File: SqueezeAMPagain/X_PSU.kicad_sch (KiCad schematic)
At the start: 1 part, among them J11 Conn_02x06_Odd_Even

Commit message: Update SqueezeAMPagain.kicad_pcb, SqueezeAMPagain.kicad_prl, SqueezeAMPagain.kicad_pro, and 7 more files
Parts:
- removed J11: Conn_02x06_Odd_Even, Connector_IDC:IDC-Header_2x06_P2.54mm_Vertical, symbol Connector_Generic:Conn_02x06_Odd_Even
- added J10: Conn_02x07_Odd_Even, Connector_IDC:IDC-Header_2x07_P2.54mm_Vertical, symbol Connector_Generic:Conn_02x07_Odd_Even
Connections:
- net +3.3V: now also J10.10 (Pin_10)
- net GND: now also J10.13 (Pin_13), J10.14 (Pin_14)
- net LV_ON: now also J10.8 (Pin_8)
- net PGND: now also J10.5 (Pin_5), J10.6 (Pin_6)
- net PON: now also J10.9 (Pin_9)
- net PVDD: now also J10.3 (Pin_3), J10.4 (Pin_4)
- net V_{IN}: now also J10.1 (Pin_1), J10.2 (Pin_2)
- net ~{WAKE}: now also J10.7 (Pin_7)
- new net SCL: J10.11 (Pin_11)
- new net SDA: J10.12 (Pin_12)
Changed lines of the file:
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@@
 	(wire
 		(pts
-			(xy 109.22 82.55) (xy 107.95 82.55)
+			(xy 109.22 85.09) (xy 107.95 85.09)
+		)
+		(stroke
+			(width 0)
+			(type default)
+		)
+	)
+	(wire
+		(pts
+			(xy 127 82.55) (xy 121.92 82.55)
 		)
 		(stroke
@@
 	(wire
 		(pts
-			(xy 121.92 82.55) (xy 124.46 82.55)
+			(xy 121.92 85.09) (xy 124.46 85.09)
 		)
 		(stroke
@@
 	(wire
 		(pts
-			(xy 124.46 82.55) (xy 124.46 85.09)
+			(xy 124.46 85.09) (xy 124.46 88.9)
 		)
 		(stroke
@@
 	(wire
 		(pts
+			(xy 105.41 82.55) (xy 109.22 82.55)
+		)
+		(stroke
+			(width 0)
+			(type default)
+		)
+	)
+	(wire
+		(pts
 			(xy 101.6 69.85) (xy 101.6 62.23)
 		)
@@
 	(wire
 		(pts
-			(xy 107.95 82.55) (xy 107.95 85.09)
+			(xy 107.95 85.09) (xy 107.95 87.63)
 		)
 		(stroke
@@
 		)
 	)
+	(hierarchical_label "SDA"
+		(shape bidirectional)
+		(at 127 82.55 0)
+		(fields_autoplaced yes)
+		(effects
+			(font
+				(size 1.27 1.27)
+			)
+			(justify left)
+		)
+	)
 	(hierarchical_label "LV_ON"
 		(shape input)
@@
 		)
 	)
+	(hierarchical_label "SCL"
+		(shape input)
+		(at 105.41 82.55 180)
+		(fields_autoplaced yes)
+		(effects
+			(font
+				(size 1.27 1.27)
+			)
+			(justify right)
+		)
+	)
 	(hierarchical_label "PON"
 		(shape input)
@@
 	)
 	(symbol
-		(lib_id "Connector_Generic:Conn_02x06_Odd_Even")
-		(at 114.3 74.93 0)
+		(lib_id "Connector_Generic:Conn_02x07_Odd_Even")
+		(at 114.3 77.47 0)
 		(unit 1)
 		(exclude_from_sim no)
@@
 		(dnp no)
 		(fields_autoplaced yes)
-		(property "Reference" "J11"
+		(property "Reference" "J10"
 			(at 115.57 63.5 0)
 			(effects
@@
 			)
 		)
-		(property "Value" "Conn_02x06_Odd_Even"
+		(property "Value" "Conn_02x07_Odd_Even"
 			(at 115.57 66.04 0)
 			(effects
@@
 			)
 		)
-		(property "Footprint" "Connector_IDC:IDC-Header_2x06_P2.54mm_Vertical"
-			(at 114.3 74.93 0)
+		(property "Footprint" "Connector_IDC:IDC-Header_2x07_P2.54mm_Vertical"
+			(at 114.3 77.47 0)
 			(effects
 				(font
@@
 		)
 		(property "Datasheet" "~"
-			(at 114.3 74.93 0)
-			(effects
-				(font
-					(size 1.27 1.27)
-				)
-				(hide yes)
-			)
-		)
-		(property "Description" "Generic connector, double row, 02x06, odd/even pin numbering scheme (row 1 odd numbers, row 2 even numbers), script generated (kicad-library-utils/schlib/autogen/connector/)"
-			(at 114.3 74.93 0)
-			(effects
-				(font
-					(size 1.27 1.27)
-				)
-				(hide yes)
-			)
+			(at 114.3 77.47 0)
+			(effects
+				(font
+					(size 1.27 1.27)
+				)
+				(hide yes)
+			)
+		)
+		(property "Description" "Generic connector, double row, 02x07, odd/even pin numbering scheme (row 1 odd numbers, row 2 even numbers), script generated (kicad-library-utils/schlib/autogen/connector/)"
+			(at 114.3 77.47 0)
+			(effects
+				(font
+					(size 1.27 1.27)
+				)
+				(hide yes)
+			)
+		)
+		(property "reichelt#" "BKL 10120556"
+			(at 114.3 77.47 0)
+			(effects
+				(font
+					(size 1.27 1.27)
+				)
+				(hide yes)
+			)
+		)
+		(pin "13"
+		)
+		(pin "5"
 		)
 		(pin "7"
 		)
-		(pin "5"
+		(pin "6"
+		)
+		(pin "10"
+		)
+		(pin "1"
+		)
+		(pin "3"
+		)
+		(pin "11"
+		)
+		(pin "8"
+		)
+		(pin "12"
 		)
 		(pin "4"
 		)
-		(pin "11"
-		)
-		(pin "8"
-		)
-		(pin "6"
-		)
 		(pin "9"
 		)
 		(pin "2"
 		)
-		(pin "10"
-		)
-		(pin "3"
-		)
-		(pin "12"
-		)
-		(pin "1"
+		(pin "14"
 		)
 		(instances
 			(project ""
 				(path "/3675160b-d9e5-490e-b506-2a7966e79ed0/ebd96d54-3bca-4cd9-8a7f-03e0b2610c15"
-					(reference "J11")
+					(reference "J10")
 					(unit 1)
 				)
@@
 	(symbol
 		(lib_id "power:GND")
-		(at 107.95 85.09 0)
+		(at 107.95 87.63 0)
 		(unit 1)
 		(exclude_from_sim no)
@@
 		(dnp no)
 		(property "Reference" "#PWR0116"
-			(at 107.95 91.44 0)
+			(at 107.95 93.98 0)
 			(effects
 				(font
@@
 		)
 		(property "Value" "GND"
-			(at 108.204 89.154 0)
+			(at 108.204 91.694 0)
 			(effects
 				(font
@@
 		)
 		(property "Footprint" ""
-			(at 107.95 85.09 0)
+			(at 107.95 87.63 0)
 			(effects
 				(font
@@
 		)
 		(property "Datasheet" ""
-			(at 107.95 85.09 0)
+			(at 107.95 87.63 0)
 			(effects
 				(font
@@
 		)
 		(property "Description" "Power symbol creates a global label with name \"GND\" , ground"
-			(at 107.95 85.09 0)
+			(at 107.95 87.63 0)
 			(effects
 				(font
@@
 	(symbol
 		(lib_id "power:GND")
-		(at 124.46 85.09 0)
+		(at 124.46 88.9 0)
 		(unit 1)
 		(exclude_from_sim no)
@@
 		(dnp no)
 		(property "Reference" "#PWR0117"
-			(at 124.46 91.44 0)
+			(at 124.46 95.25 0)
 			(effects
 				(font
@@
 		)
 		(property "Value" "GND"
-			(at 124.714 89.154 0)
+			(at 124.714 92.964 0)
 			(effects
 				(font
@@
 		)
 		(property "Footprint" ""
-			(at 124.46 85.09 0)
+			(at 124.46 88.9 0)
 			(effects
 				(font
@@
 		)
 		(property "Datasheet" ""
-			(at 124.46 85.09 0)
+			(at 124.46 88.9 0)
 			(effects
 				(font
@@
 		)
 		(property "Description" "Power symbol creates a global label with name \"GND\" , ground"
-			(at 124.46 85.09 0)
-			(effects
-				(font
+			(at 124.46 88.9 0)
+			(effects
+				(font

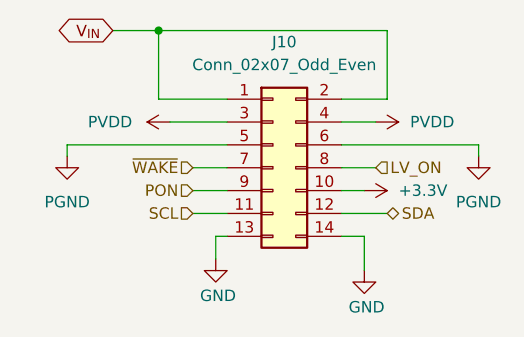
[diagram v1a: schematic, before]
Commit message: Update SqueezeAMPagain.kicad_pcb, SqueezeAMPagain.kicad_prl, SqueezeAMPagain.kicad_pro, and 5 more files
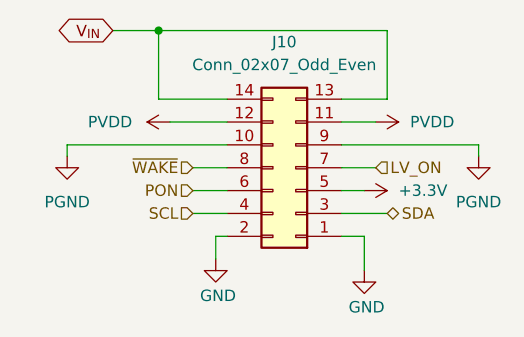
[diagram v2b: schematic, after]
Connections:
- net +3.3V: now also J10.5 (Pin_5); no longer J10.10 (Pin_10)
- net GND: now also J10.1 (Pin_1), J10.2 (Pin_2); no longer J10.13 (Pin_13), J10.14 (Pin_14)
- net LV_ON: now also J10.7 (Pin_7); no longer J10.8 (Pin_8)
- net PGND: now also J10.10 (Pin_10), J10.9 (Pin_9); no longer J10.5 (Pin_5), J10.6 (Pin_6)
- net PON: now also J10.6 (Pin_6); no longer J10.9 (Pin_9)
- net PVDD: now also J10.11 (Pin_11), J10.12 (Pin_12); no longer J10.3 (Pin_3), J10.4 (Pin_4)
- net SCL: now also J10.4 (Pin_4); no longer J10.11 (Pin_11)
- net SDA: now also J10.3 (Pin_3); no longer J10.12 (Pin_12)
- net V_{IN}: now also J10.13 (Pin_13), J10.14 (Pin_14); no longer J10.1 (Pin_1), J10.2 (Pin_2)
- net ~{WAKE}: now also J10.8 (Pin_8); no longer J10.7 (Pin_7)
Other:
- moved on the sheet: J10
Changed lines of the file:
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@@
 	(symbol
 		(lib_id "Connector_Generic:Conn_02x07_Odd_Even")
-		(at 114.3 77.47 0)
+		(at 116.84 77.47 180)
 		(unit 1)
 		(exclude_from_sim no)
@@
 		)
 		(property "Footprint" "Connector_IDC:IDC-Header_2x07_P2.54mm_Vertical"
-			(at 114.3 77.47 0)
+			(at 116.84 77.47 0)
 			(effects
 				(font
@@
 		)
 		(property "Datasheet" "~"
-			(at 114.3 77.47 0)
+			(at 116.84 77.47 0)
 			(effects
 				(font
@@
 		)
 		(property "Description" "Generic connector, double row, 02x07, odd/even pin numbering scheme (row 1 odd numbers, row 2 even numbers), script generated (kicad-library-utils/schlib/autogen/connector/)"
-			(at 114.3 77.47 0)
+			(at 116.84 77.47 0)
 			(effects
 				(font
@@
 		)
 		(property "reichelt#" "BKL 10120556"
-			(at 114.3 77.47 0)
+			(at 116.84 77.47 0)
 			(effects
 				(font

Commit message: Update SqueezeAMPagain.kicad_pcb, SqueezeAMPagain.kicad_prl, SqueezeAMPagain.kicad_pro, and 4 more files
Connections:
- net +3.3V: now also J10.10 (Pin_10); no longer J10.5 (Pin_5)
- net GND: now also J10.13 (Pin_13), J10.14 (Pin_14); no longer J10.1 (Pin_1), J10.2 (Pin_2)
- net LV_ON: now also J10.8 (Pin_8); no longer J10.7 (Pin_7)
- net PGND: now also J10.5 (Pin_5), J10.6 (Pin_6); no longer J10.10 (Pin_10), J10.9 (Pin_9)
- net PON: now also J10.9 (Pin_9); no longer J10.6 (Pin_6)
- net PVDD: now also J10.3 (Pin_3), J10.4 (Pin_4); no longer J10.11 (Pin_11), J10.12 (Pin_12)
- net SCL: now also J10.11 (Pin_11); no longer J10.4 (Pin_4)
- net SDA: now also J10.12 (Pin_12); no longer J10.3 (Pin_3)
- net V_{IN}: now also J10.1 (Pin_1); no longer J10.13 (Pin_13), J10.14 (Pin_14)
- net ~{WAKE}: now also J10.7 (Pin_7); no longer J10.8 (Pin_8)
- new net V_{USB}: J10.2 (Pin_2)
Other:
- moved on the sheet: J10

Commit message: Update SqueezeAMPagain.kicad_pcb, SqueezeAMPagain.kicad_prl, SqueezeAMPagain.kicad_pro, and 5 more files
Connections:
- net PVDD is gone; now on net V_{IN}: J10.3 (Pin_3), J10.4 (Pin_4)
- net V_{IN}: no longer J10.1 (Pin_1)
- new net V_{supply}: J10.1 (Pin_1)
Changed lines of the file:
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@@
+		)
+	)
+	(global_label "V_{supply}"
+		(shape input)
+		(at 109.22 90.17 180)
+		(fields_autoplaced yes)
+		(effects
+			(font
+				(size 1.27 1.27)
+			)
+			(justify right)
+		)
+		(property "Intersheetrefs" "${INTERSHEET_REFS}"
+			(at 100.209 90.17 0)
+			(effects
+				(font
+					(size 1.27 1.27)
+				)
+				(justify right)
+				(hide yes)
+			)
 		)
 	)
@@
 	)
 	(global_label "V_{IN}"
-		(shape bidirectional)
-		(at 109.22 90.17 180)
+		(shape output)
+		(at 148.59 92.71 0)
+		(fields_autoplaced yes)
+		(effects
+			(font
+				(size 1.27 1.27)
+			)
+			(justify left)
+		)
+		(property "Intersheetrefs" "${INTERSHEET_REFS}"
+			(at 154.2628 92.71 0)
+			(effects
+				(font
+					(size 1.27 1.27)
+				)
+				(justify left)
+				(hide yes)
+			)
+		)
+	)
+	(global_label "V_{IN}"
+		(shape output)
+		(at 125.73 92.71 180)
 		(fields_autoplaced yes)
 		(effects
@@
 		)
 		(property "Intersheetrefs" "${INTERSHEET_REFS}"
-			(at 102.4359 90.17 0)
+			(at 120.0572 92.71 0)
 			(effects
 				(font
@@
 	)
 	(symbol
-		(lib_id "power:+24V")
-		(at 148.59 92.71 270)
-		(unit 1)
-		(exclude_from_sim no)
-		(in_bom yes)
-		(on_board yes)
-		(dnp no)
-		(fields_autoplaced yes)
-		(property "Reference" "#PWR0119"
-			(at 144.78 92.71 0)
-			(effects
-				(font
-					(size 1.27 1.27)
-				)
-				(hide yes)
-			)
-		)
-		(property "Value" "PVDD"
-			(at 152.4 92.7099 90)
-			(effects
-				(font
-					(size 1.27 1.27)
-				)
-				(justify left)
-			)
-		)
-		(property "Footprint" ""
-			(at 148.59 92.71 0)
-			(effects
-				(font
-					(size 1.27 1.27)
-				)
-				(hide yes)
-			)
-		)
-		(property "Datasheet" ""
-			(at 148.59 92.71 0)
-			(effects
-				(font
-					(size 1.27 1.27)
-				)
-				(hide yes)
-			)
-		)
-		(property "Description" "Power symbol creates a global label with name \"+24V\""
-			(at 148.59 92.71 0)
-			(effects
-				(font
-					(size 1.27 1.27)
-				)
-				(hide yes)
-			)
-		)
-		(pin "1"
-		)
-		(instances
-			(project "SqueezeAMPagain"
-				(path "/3675160b-d9e5-490e-b506-2a7966e79ed0/ebd96d54-3bca-4cd9-8a7f-03e0b2610c15"
-					(reference "#PWR0119")
-					(unit 1)
-				)
-			)
-		)
-	)
-	(symbol
 		(lib_id "power:GND")
 		(at 147.32 109.22 0)
@@
 					(unit 1)
 				)
-			)
-		)
-	)
-	(symbol
-		(lib_id "power:+24V")
-		(at 125.73 92.71 90)
-		(unit 1)
-		(exclude_from_sim no)
-		(in_bom yes)
-		(on_board yes)
-		(dnp no)
-		(fields_autoplaced yes)
-		(property "Reference" "#PWR0115"
-			(at 129.54 92.71 0)
-			(effects
-				(font
-					(size 1.27 1.27)
-				)
-				(hide yes)
-			)
-		)
-		(property "Value" "PVDD"
-			(at 121.531 92.7099 90)
-			(effects
-				(font
-					(size 1.27 1.27)
-				)
-				(justify left)
-			)
-		)
-		(property "Footprint" ""
-			(at 125.73 92.71 0)
-			(effects
-				(font
-					(size 1.27 1.27)
-				)
-				(hide yes)
-			)
-		)
-		(property "Datasheet" ""
-			(at 125.73 92.71 0)
-			(effects
-				(font
-					(size 1.27 1.27)
-				)
-				(hide yes)
-			)
-		)
-		(property "Description" "Power symbol creates a global label with name \"+24V\""
-			(at 125.73 92.71 0)
-			(effects
-				(font
-					(size 1.27 1.27)
-				)
-				(hide yes)
-			)
-		)
-		(pin "1"
-		)
-		(instances
-			(project "SqueezeAMPagain"
-				(path "/3675160b-d9e5-490e-b506-2a7966e79ed0/ebd96d54-3bca-4cd9-8a7f-03e0b2610c15"
-					(reference "#PWR0115")
-					(unit 1)
-				)

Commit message: Update SqueezeAMPagain.kicad_pcb, SqueezeAMPagain.kicad_prl, SqueezeAMPagain.kicad_pro, and 11 more files
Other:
- note added: "Power expansion connector"
- title: (none) -> SqueezeAMP_{again}
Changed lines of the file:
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@@
 	(generator_version "8.0")
 	(paper "A4")
-	(wire
-		(pts
-			(xy 125.73 92.71) (xy 132.08 92.71)
+	(title_block
+		(title "SqueezeAMP_{again}")
+		(date "2024-08-23")
+		(rev "1.0")
+	)
+	(wire
+		(pts
+			(xy 119.38 92.71) (xy 132.08 92.71)
 		)
 		(stroke
@@
 	(wire
 		(pts
-			(xy 132.08 105.41) (xy 130.81 105.41)
+			(xy 132.08 105.41) (xy 129.54 105.41)
 		)
 		(stroke
@@
 	(wire
 		(pts
-			(xy 114.3 96.52) (xy 114.3 95.25)
+			(xy 101.6 96.52) (xy 101.6 95.25)
 		)
 		(stroke
@@
 	(wire
 		(pts
-			(xy 160.02 95.25) (xy 144.78 95.25)
-		)
-		(stroke
-			(width 0)
-			(type default)
-		)
-	)
-	(wire
-		(pts
-			(xy 114.3 95.25) (xy 132.08 95.25)
-		)
-		(stroke
-			(width 0)
-			(type default)
-		)
-	)
-	(wire
-		(pts
-			(xy 144.78 92.71) (xy 148.59 92.71)
-		)
-		(stroke
-			(width 0)
-			(type default)
-		)
-	)
-	(wire
-		(pts
-			(xy 160.02 96.52) (xy 160.02 95.25)
-		)
-		(stroke
-			(width 0)
-			(type default)
-		)
-	)
-	(wire
-		(pts
-			(xy 130.81 105.41) (xy 130.81 109.22)
-		)
-		(stroke
-			(width 0)
-			(type default)
+			(xy 179.07 95.25) (xy 144.78 95.25)
+		)
+		(stroke
+			(width 0)
+			(type default)
+		)
+	)
+	(wire
+		(pts
+			(xy 101.6 95.25) (xy 132.08 95.25)
+		)
+		(stroke
+			(width 0)
+			(type default)
+		)
+	)
+	(wire
+		(pts
+			(xy 144.78 92.71) (xy 157.48 92.71)
+		)
+		(stroke
+			(width 0)
+			(type default)
+		)
+	)
+	(wire
+		(pts
+			(xy 179.07 96.52) (xy 179.07 95.25)
+		)
+		(stroke
+			(width 0)
+			(type default)
+		)
+	)
+	(wire
+		(pts
+			(xy 129.54 105.41) (xy 129.54 109.22)
+		)
+		(stroke
+			(width 0)
+			(type default)
+		)
+	)
+	(text "Power expansion connector"
+		(exclude_from_sim no)
+		(at 138.43 73.406 0)
+		(effects
+			(font
+				(size 1.27 1.27)
+			)
 		)
 	)
@@
 	(global_label "V_{IN}"
 		(shape output)
-		(at 148.59 92.71 0)
+		(at 157.48 92.71 0)
 		(fields_autoplaced yes)
 		(effects
@@
 		)
 		(property "Intersheetrefs" "${INTERSHEET_REFS}"
-			(at 154.2628 92.71 0)
+			(at 163.1528 92.71 0)
 			(effects
 				(font
@@
 	(global_label "V_{IN}"
 		(shape output)
-		(at 125.73 92.71 180)
+		(at 119.38 92.71 180)
 		(fields_autoplaced yes)
 		(effects
@@
 		)
 		(property "Intersheetrefs" "${INTERSHEET_REFS}"
-			(at 120.0572 92.71 0)
+			(at 113.7072 92.71 0)
 			(effects
 				(font
@@
 	(symbol
 		(lib_id "power:GND1")
-		(at 114.3 96.52 0)
+		(at 101.6 96.52 0)
 		(unit 1)
 		(exclude_from_sim no)
@@
 		(fields_autoplaced yes)
 		(property "Reference" "#PWR0114"
-			(at 114.3 102.87 0)
+			(at 101.6 102.87 0)
 			(effects
 				(font
@@
 		)
 		(property "Value" "PGND"
-			(at 114.3 101.6 0)
+			(at 101.6 101.6 0)
 			(effects
 				(font
@@
 		)
 		(property "Footprint" ""
-			(at 114.3 96.52 0)
+			(at 101.6 96.52 0)
 			(effects
 				(font
@@
 		)
 		(property "Datasheet" ""
-			(at 114.3 96.52 0)
+			(at 101.6 96.52 0)
 			(effects
 				(font
@@
 		)
 		(property "Description" "Power symbol creates a global label with name \"GND1\" , ground"
-			(at 114.3 96.52 0)
+			(at 101.6 96.52 0)
 			(effects
 				(font
@@
 	(symbol
 		(lib_id "power:GND")
-		(at 130.81 109.22 0)
+		(at 129.54 109.22 0)
 		(unit 1)
 		(exclude_from_sim no)
@@
 		(dnp no)
 		(property "Reference" "#PWR0116"
-			(at 130.81 115.57 0)
+			(at 129.54 115.57 0)
 			(effects
 				(font
@@
 		)
 		(property "Value" "GND"
-			(at 131.064 113.284 0)
+			(at 129.794 113.284 0)
 			(effects
 				(font
@@
 		)
 		(property "Footprint" ""
-			(at 130.81 109.22 0)
+			(at 129.54 109.22 0)
 			(effects
 				(font
@@
 		)
 		(property "Datasheet" ""
-			(at 130.81 109.22 0)
+			(at 129.54 109.22 0)
 			(effects
 				(font
@@
 		)
 		(property "Description" "Power symbol creates a global label with name \"GND\" , ground"
-			(at 130.81 109.22 0)
+			(at 129.54 109.22 0)
 			(effects
 				(font
@@
 	(symbol
 		(lib_id "power:GND1")
-		(at 160.02 96.52 0)
+		(at 179.07 96.52 0)
 		(unit 1)
 		(exclude_from_sim no)
@@
 		(fields_autoplaced yes)
 		(property "Reference" "#PWR0120"
-			(at 160.02 102.87 0)
+			(at 179.07 102.87 0)
 			(effects
 				(font
@@
 		)
 		(property "Value" "PGND"
-			(at 160.02 101.6 0)
+			(at 179.07 101.6 0)
 			(effects
 				(font
@@
 		)
 		(property "Footprint" ""
-			(at 160.02 96.52 0)
+			(at 179.07 96.52 0)
 			(effects
 				(font
@@
 		)
 		(property "Datasheet" ""
-			(at 160.02 96.52 0)
+			(at 179.07 96.52 0)
 			(effects
 				(font
@@
 		)
 		(property "Description" "Power symbol creates a global label with name \"GND1\" , ground"
-			(at 160.02 96.52 0)
-			(effects
-				(font
+			(at 179.07 96.52 0)
+			(effects
+				(font

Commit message: v2
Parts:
- renumbered J10 to J9
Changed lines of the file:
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@@
 		(dnp no)
 		(fields_autoplaced yes)
-		(property "Reference" "J10"
+		(property "Reference" "J9"
 			(at 138.43 83.82 0)
 			(effects
@@
 			(project ""
 				(path "/3675160b-d9e5-490e-b506-2a7966e79ed0/ebd96d54-3bca-4cd9-8a7f-03e0b2610c15"
-					(reference "J10")
+					(reference "J9")
 					(unit 1)
 				)
@@
 		(dnp no)
 		(fields_autoplaced yes)
-		(property "Reference" "#PWR0114"
+		(property "Reference" "#PWR0111"
 			(at 101.6 102.87 0)
 			(effects
@@
 			(project "SqueezeAMPagain"
 				(path "/3675160b-d9e5-490e-b506-2a7966e79ed0/ebd96d54-3bca-4cd9-8a7f-03e0b2610c15"
-					(reference "#PWR0114")
+					(reference "#PWR0111")
 					(unit 1)
 				)
@@
 		(dnp no)
 		(fields_autoplaced yes)
-		(property "Reference" "#PWR0117"
+		(property "Reference" "#PWR0113"
 			(at 143.51 100.33 0)
 			(effects
@@
 			(project "SqueezeAMPagain"
 				(path "/3675160b-d9e5-490e-b506-2a7966e79ed0/ebd96d54-3bca-4cd9-8a7f-03e0b2610c15"
-					(reference "#PWR0117")
+					(reference "#PWR0113")
 					(unit 1)
 				)
@@
 		(on_board yes)
 		(dnp no)
-		(property "Reference" "#PWR0116"
+		(property "Reference" "#PWR0112"
 			(at 129.54 115.57 0)
 			(effects
@@
 			(project "SqueezeAMPagain"
 				(path "/3675160b-d9e5-490e-b506-2a7966e79ed0/ebd96d54-3bca-4cd9-8a7f-03e0b2610c15"
-					(reference "#PWR0116")
+					(reference "#PWR0112")
 					(unit 1)
 				)
@@
 		(on_board yes)
 		(dnp no)
-		(property "Reference" "#PWR0118"
+		(property "Reference" "#PWR0114"
 			(at 147.32 115.57 0)
 			(effects
@@
 			(project "SqueezeAMPagain"
 				(path "/3675160b-d9e5-490e-b506-2a7966e79ed0/ebd96d54-3bca-4cd9-8a7f-03e0b2610c15"
-					(reference "#PWR0118")
+					(reference "#PWR0114")
 					(unit 1)
 				)
@@
 		(dnp no)
 		(fields_autoplaced yes)
-		(property "Reference" "#PWR0120"
+		(property "Reference" "#PWR0115"
 			(at 179.07 102.87 0)
 			(effects
@@
 			(project "SqueezeAMPagain"
 				(path "/3675160b-d9e5-490e-b506-2a7966e79ed0/ebd96d54-3bca-4cd9-8a7f-03e0b2610c15"
-					(reference "#PWR0120")
-					(unit 1)
-				)
+					(reference "#PWR0115")
+					(unit 1)
+				)
